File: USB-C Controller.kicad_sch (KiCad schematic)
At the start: 15 parts, among them J3 USB_C_Receptacle, Q5 AO4459, U3 STUSB4500QTR

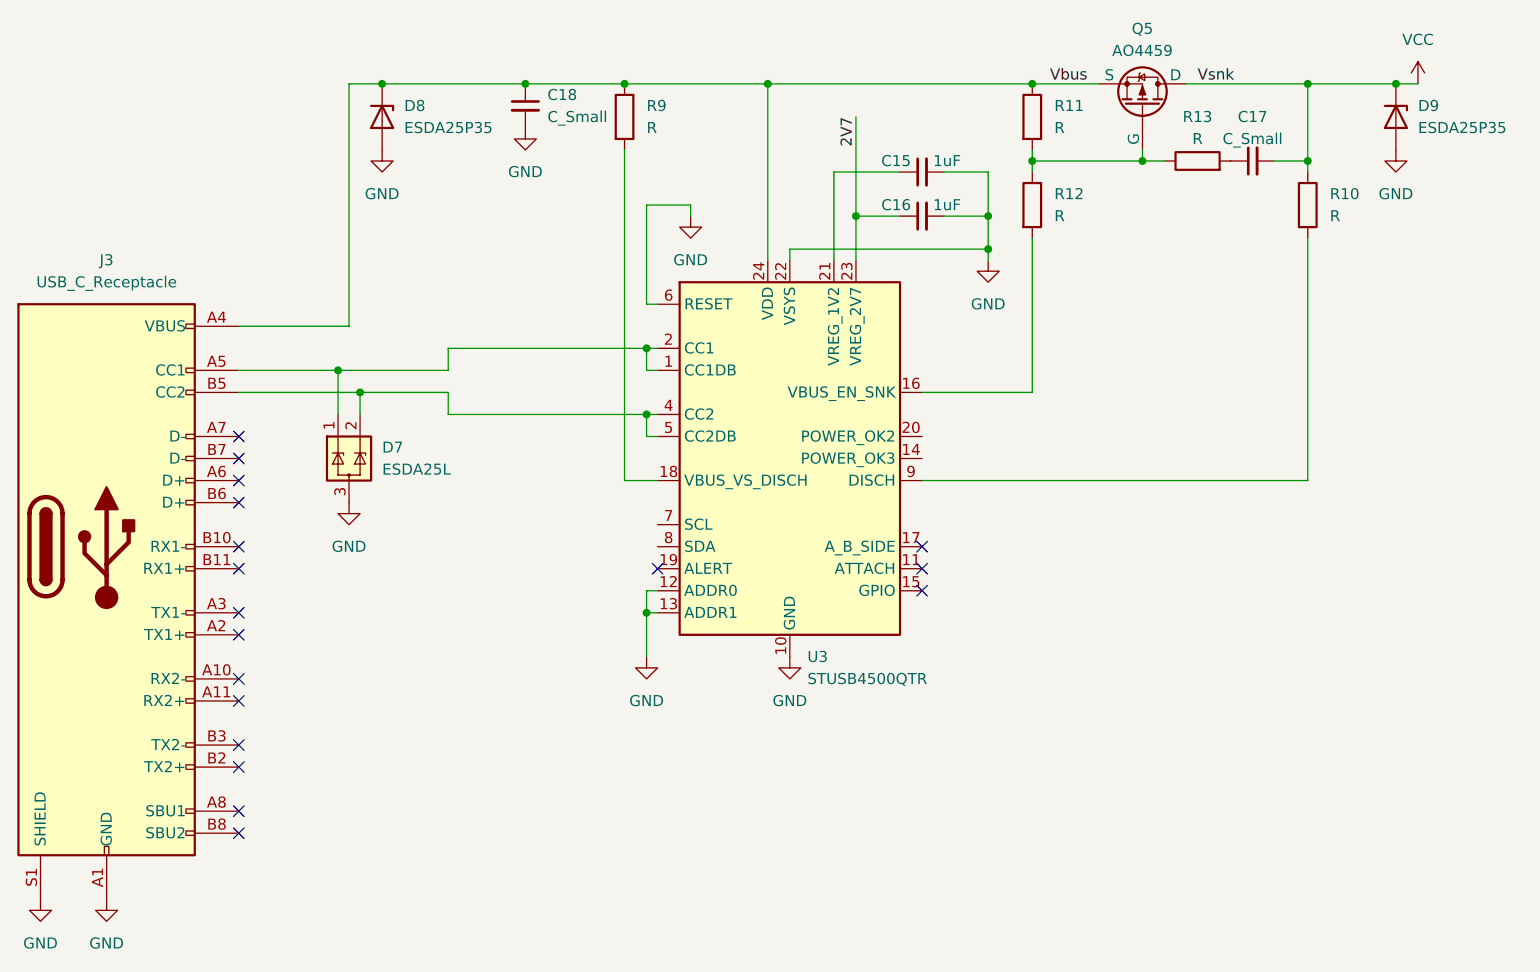
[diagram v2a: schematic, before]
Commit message: Add ESD protection, I2C header, and specify passives
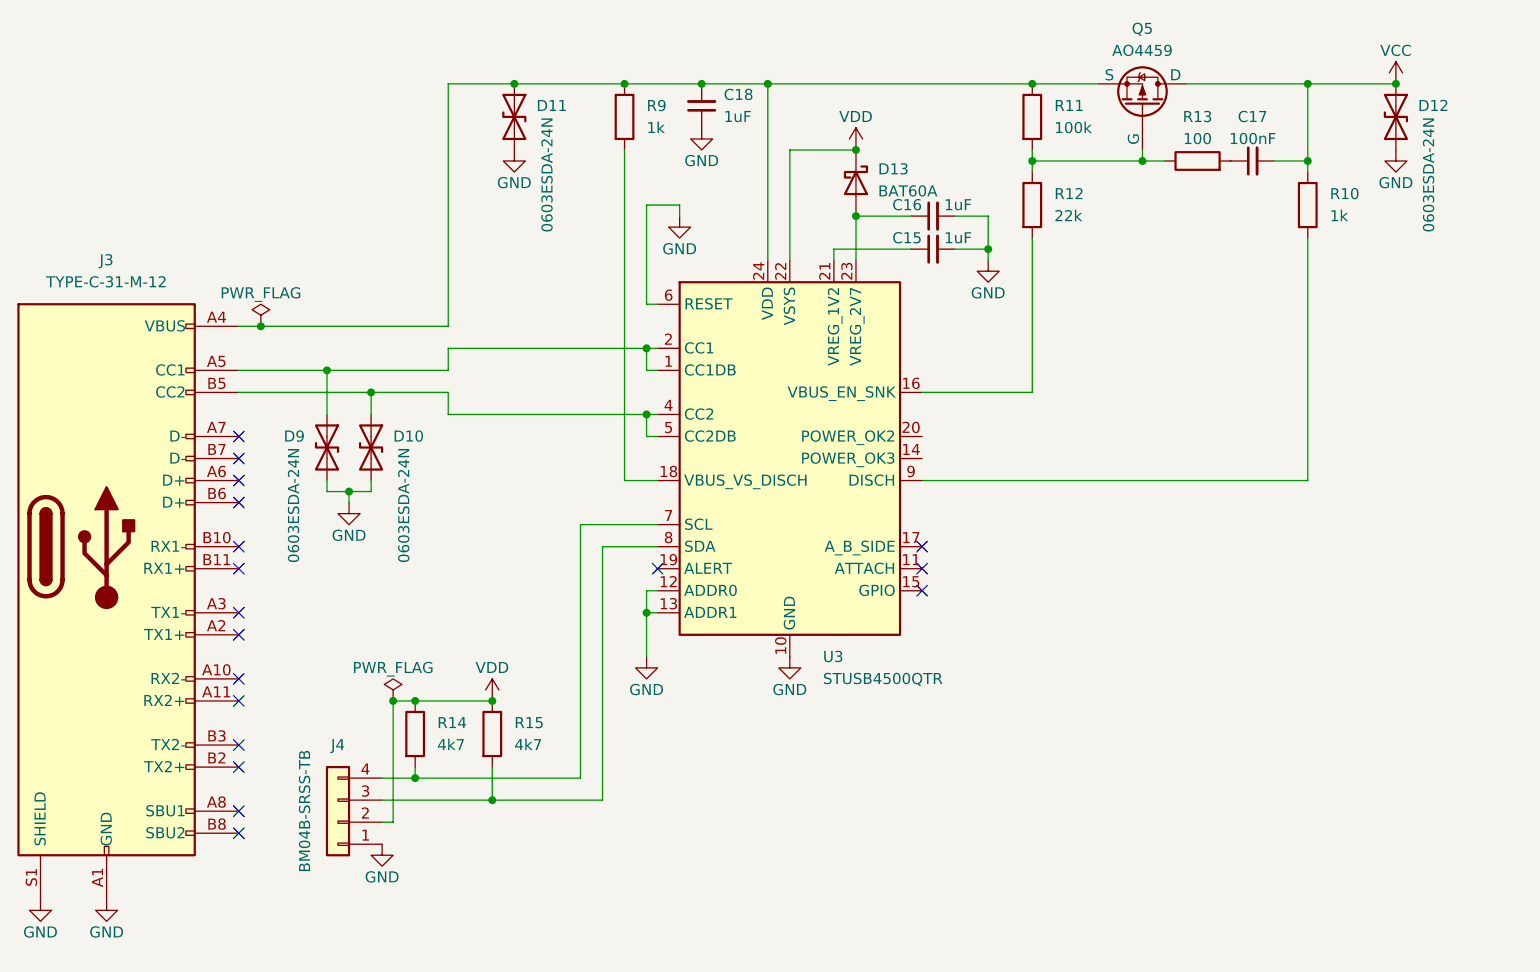
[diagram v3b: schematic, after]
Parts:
- removed D7: ESDA25L, Package_TO_SOT_SMD:SOT-23, symbol BRAUNIT Charger:ESDA25L
- removed D8, D9: ESDA25P35, symbol Device:D_Zener
- added D10, D11, D12, D9: 0603ESDA-24N, Diode_SMD:D_0603_1608Metric, symbol Device:D_TVS
- added D13: BAT60A, Diode_SMD:D_SOD-323, symbol Diode:BAT60A
- added J4: BM04B-SRSS-TB, Connector_JST:JST_SH_BM04B-SRSS-TB_1x04-1MP_P1.00mm_Vertical, symbol Connector_Generic:Conn_01x04
- added R14, R15: 4k7, Resistor_SMD:R_0603_1608Metric, symbol Device:R
- C17: value C_Small -> 100nF; footprint (none) -> Capacitor_SMD:C_0603_1608Metric; LCSC (none) -> C14663
- C18: value C_Small -> 1uF; footprint (none) -> Capacitor_SMD:C_0805_2012Metric; LCSC (none) -> C91185
- J3: value USB_C_Receptacle -> TYPE-C-31-M-12
- R10, R9: value R -> 1k; footprint (none) -> Resistor_SMD:R_0603_1608Metric; LCSC (none) -> C22548
- R11: value R -> 100k; footprint (none) -> Resistor_SMD:R_0603_1608Metric; LCSC (none) -> C14675
- R12: value R -> 22k; footprint (none) -> Resistor_SMD:R_0603_1608Metric; LCSC (none) -> C114065
- R13: value R -> 100; footprint (none) -> Resistor_SMD:R_0603_1608Metric; LCSC (none) -> C105588
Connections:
- net GND: now also C18.1, D10.2 (A2), D11.2 (A2), D12.2 (A2), D9.2 (A2), J4.1 (Pin_1); no longer C18.2, U3.22 (VSYS)
- net VCC: now also D12.1 (A1)
- net at J3.A5 (CC1), U3.1 (CC1DB), U3.2 (CC1): now also D9.1 (A1)
- net at J3.B5 (CC2), U3.4 (CC2), U3.5 (CC2DB): now also D10.1 (A1)
- net at U3.7 (SCL): now also J4.4 (Pin_4), R14.2
- net at U3.8 (SDA): now also J4.3 (Pin_3), R15.2
- net 2V7: no longer names the net of C16.1, U3.23 (VREG_2V7)
- net 2V7: now also D13.2 (A)
- net Vbus: no longer names the net of J3.A4 (VBUS), J3.A9 (VBUS), J3.B4 (VBUS), J3.B9 (VBUS), Q5.1 (S), Q5.2 (S), Q5.3 (S), R11.1, R9.1, U3.24 (VDD)
- net Vbus: now also C18.2, D11.1 (A1); no longer C18.1
- new net VDD: D13.1 (K), J4.2 (Pin_2), R14.1, R15.1, U3.22 (VSYS)
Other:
- moved on the sheet: C15, C16, C18

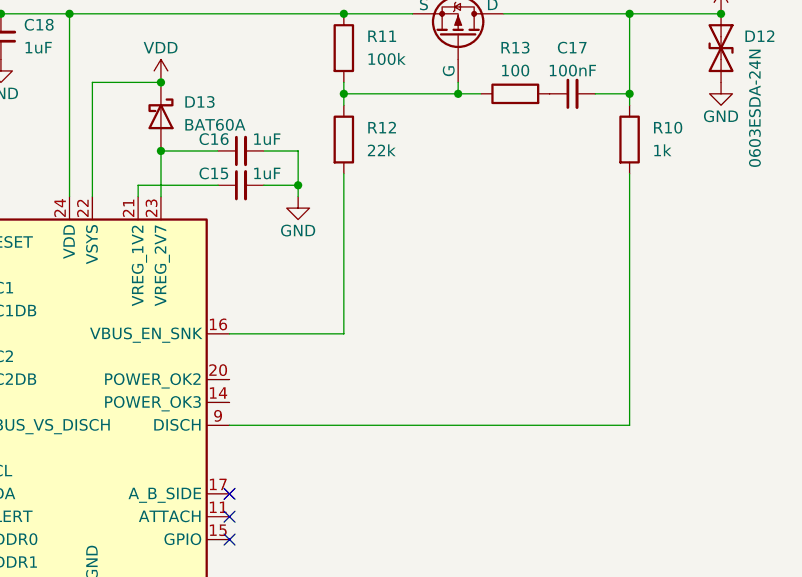
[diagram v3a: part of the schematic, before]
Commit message: Add USB-C status indicator LED and right charger enable
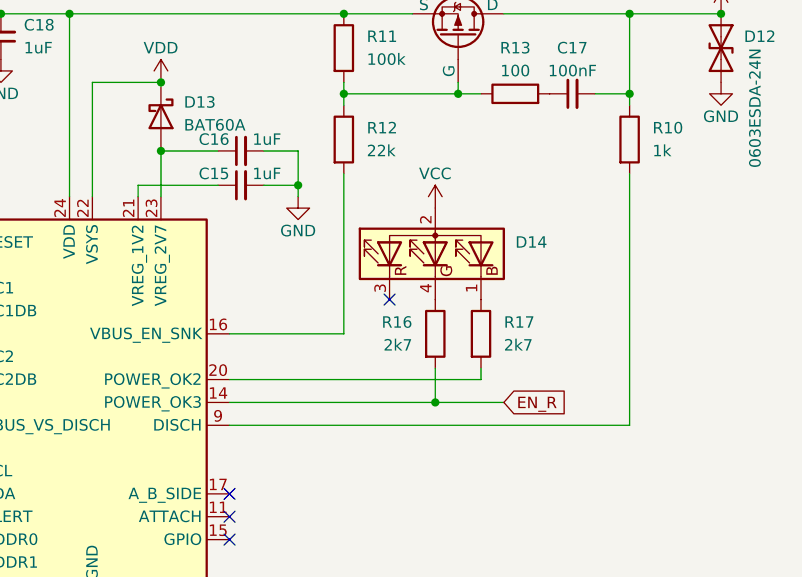
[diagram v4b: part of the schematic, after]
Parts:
- added D14: (no value), symbol Device:LED_BARG
- added R16, R17: 2k7, Resistor_SMD:R_0603_1608Metric, symbol Device:R
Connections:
- net VCC: now also D14.2 (A)
- net EN_R: now reaches U3.14 (POWER_OK3)
- net EN_R: now also R16.2
- net at U3.20 (POWER_OK2): now also R17.2
- new net: D14.1 (BK), R17.1
- new net: D14.4 (GK), R16.1
- no-connect marks 18 -> 19
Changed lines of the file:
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@@
   (junction (at 184.15 76.2) (diameter 0) (color 0 0 0 0)
   )
+  (junction (at 194.31 110.49) (diameter 0) (color 0 0 0 0)
+  )
   (junction (at 113.03 147.32) (diameter 0) (color 0 0 0 0)
   )
@@
   (junction (at 163.83 82.55) (diameter 0) (color 0 0 0 0)
   )
+  (no_connect (at 189.23 99.06))
   (no_connect (at 92.71 151.13))
   (no_connect (at 92.71 153.67))
@@
     (stroke (width 0) (type default) (color 0 0 0 0))
   )
+  (wire (pts (xy 171.45 110.49) (xy 194.31 110.49))
+    (stroke (width 0) (type default) (color 0 0 0 0))
+  )
   (wire (pts (xy 132.08 118.11) (xy 140.97 118.11))
     (stroke (width 0) (type default) (color 0 0 0 0))
@@
     (stroke (width 0) (type default) (color 0 0 0 0))
   )
+  (wire (pts (xy 194.31 110.49) (xy 201.93 110.49))
+    (stroke (width 0) (type default) (color 0 0 0 0))
+  )
   (wire (pts (xy 184.15 76.2) (xy 184.15 77.47))
     (stroke (width 0) (type default) (color 0 0 0 0))
@@
     (stroke (width 0) (type default) (color 0 0 0 0))
   )
+  (wire (pts (xy 171.45 107.95) (xy 199.39 107.95))
+    (stroke (width 0) (type default) (color 0 0 0 0))
+  )
   (wire (pts (xy 134.62 149.86) (xy 134.62 120.65))
     (stroke (width 0) (type default) (color 0 0 0 0))
@@
     (stroke (width 0) (type default) (color 0 0 0 0))
   )
+  (wire (pts (xy 194.31 106.68) (xy 194.31 110.49))
+    (stroke (width 0) (type default) (color 0 0 0 0))
+  )
   (wire (pts (xy 215.9 67.31) (xy 215.9 76.2))
     (stroke (width 0) (type default) (color 0 0 0 0))
@@
     (stroke (width 0) (type default) (color 0 0 0 0))
   )
+  (wire (pts (xy 199.39 107.95) (xy 199.39 106.68))
+    (stroke (width 0) (type default) (color 0 0 0 0))
+  )
   (wire (pts (xy 175.26 82.55) (xy 179.07 82.55))
     (stroke (width 0) (type default) (color 0 0 0 0))
@@
   (wire (pts (xy 140.97 107.95) (xy 139.7 107.95))
     (stroke (width 0) (type default) (color 0 0 0 0))
+  )
+  (global_label "EN_R" (shape input) (at 201.93 110.49 0) (fields_autoplaced)
+    (effects (font (size 1.27 1.27)) (justify left))
+    (property "Intersheet References" "${INTERSHEET_REFS}" (id 0) (at 209.0602 110.4106 0)
+      (effects (font (size 1.27 1.27)) (justify left) hide)
+    )
+  )
+  (symbol (lib_id "Device:R") (at 199.39 102.87 0) (unit 1)
+    (in_bom yes) (on_board yes) (fields_autoplaced)
+    (property "Reference" "R17" (id 0) (at 201.93 101.5999 0)
+      (effects (font (size 1.27 1.27)) (justify left))
+    )
+    (property "Value" "2k7" (id 1) (at 201.93 104.1399 0)
+      (effects (font (size 1.27 1.27)) (justify left))
+    )
+    (property "Footprint" "Resistor_SMD:R_0603_1608Metric" (id 2) (at 197.612 102.87 90)
+      (effects (font (size 1.27 1.27)) hide)
+    )
+    (property "Datasheet" "~" (id 3) (at 199.39 102.87 0)
+      (effects (font (size 1.27 1.27)) hide)
+    )
+    (property "LCSC" "C114612" (id 4) (at 199.39 102.87 0)
+      (effects (font (size 1.27 1.27)) hide)
+    )
+    (pin "1")
+    (pin "2")
   )
   (symbol (lib_id "power:GND") (at 226.06 74.93 0) (unit 1)
@@
     (pin "1")
   )
+  (symbol (lib_id "Device:LED_BARG") (at 194.31 93.98 90) (unit 1)
+    (in_bom yes) (on_board yes)
+    (property "Reference" "D14" (id 0) (at 203.2 92.71 90)
+      (effects (font (size 1.27 1.27)) (justify right))
+    )
+    (property "Value" "" (id 1) (at 196.85 88.9 90)
+      (effects (font (size 1.27 1.27)) (justify right))
+    )
+    (property "Footprint" "" (id 2) (at 195.58 93.98 0)
+      (effects (font (size 1.27 1.27)) hide)
+    )
+    (property "Datasheet" "~" (id 3) (at 195.58 93.98 0)
+      (effects (font (size 1.27 1.27)) hide)
+    )
+    (property "LCSC" "C389528" (id 4) (at 194.31 93.98 90)
+      (effects (font (size 1.27 1.27)) hide)
+    )
+    (pin "1")
+    (pin "2")
+    (pin "3")
+    (pin "4")
+  )
   (symbol (lib_id "Device:R") (at 203.2 76.2 90) (unit 1)
     (in_bom yes) (on_board yes)
@@
     (pin "2")
   )
+  (symbol (lib_id "power:VCC") (at 194.31 88.9 0) (unit 1)
+    (in_bom yes) (on_board yes)
+    (property "Reference" "#PWR0137" (id 0) (at 194.31 92.71 0)
+      (effects (font (size 1.27 1.27)) hide)
+    )
+    (property "Value" "VCC" (id 1) (at 194.31 85.09 0))
+    (property "Footprint" "" (id 2) (at 194.31 88.9 0)
+      (effects (font (size 1.27 1.27)) hide)
+    )
+    (property "Datasheet" "" (id 3) (at 194.31 88.9 0)
+      (effects (font (size 1.27 1.27)) hide)
+    )
+    (pin "1")
+  )
   (symbol (lib_id "Device:D_TVS") (at 102.87 109.22 270) (unit 1)
     (in_bom yes) (on_board yes)
@@
     )
     (pin "1")
+    (pin "2")
+  )
+  (symbol (lib_id "Device:R") (at 194.31 102.87 0) (unit 1)
+    (in_bom yes) (on_board yes)
+    (property "Reference" "R16" (id 0) (at 191.77 101.6 0)
+      (effects (font (size 1.27 1.27)) (justify right))
+    )
+    (property "Value" "2k7" (id 1) (at 191.77 104.14 0)
+      (effects (font (size 1.27 1.27)) (justify right))
+    )
+    (property "Footprint" "Resistor_SMD:R_0603_1608Metric" (id 2) (at 192.532 102.87 90)
+      (effects (font (size 1.27 1.27)) hide)
+    )
+    (property "Datasheet" "~" (id 3) (at 194.31 102.87 0)
+      (effects (font (size 1.27 1.27)) hide)
+    )
+    (property "LCSC" "C114612" (id 4) (at 194.31 102.87 0)
+      (effects (font (size 1.27 1.27)) hide)
+    )
+    (pin "1")

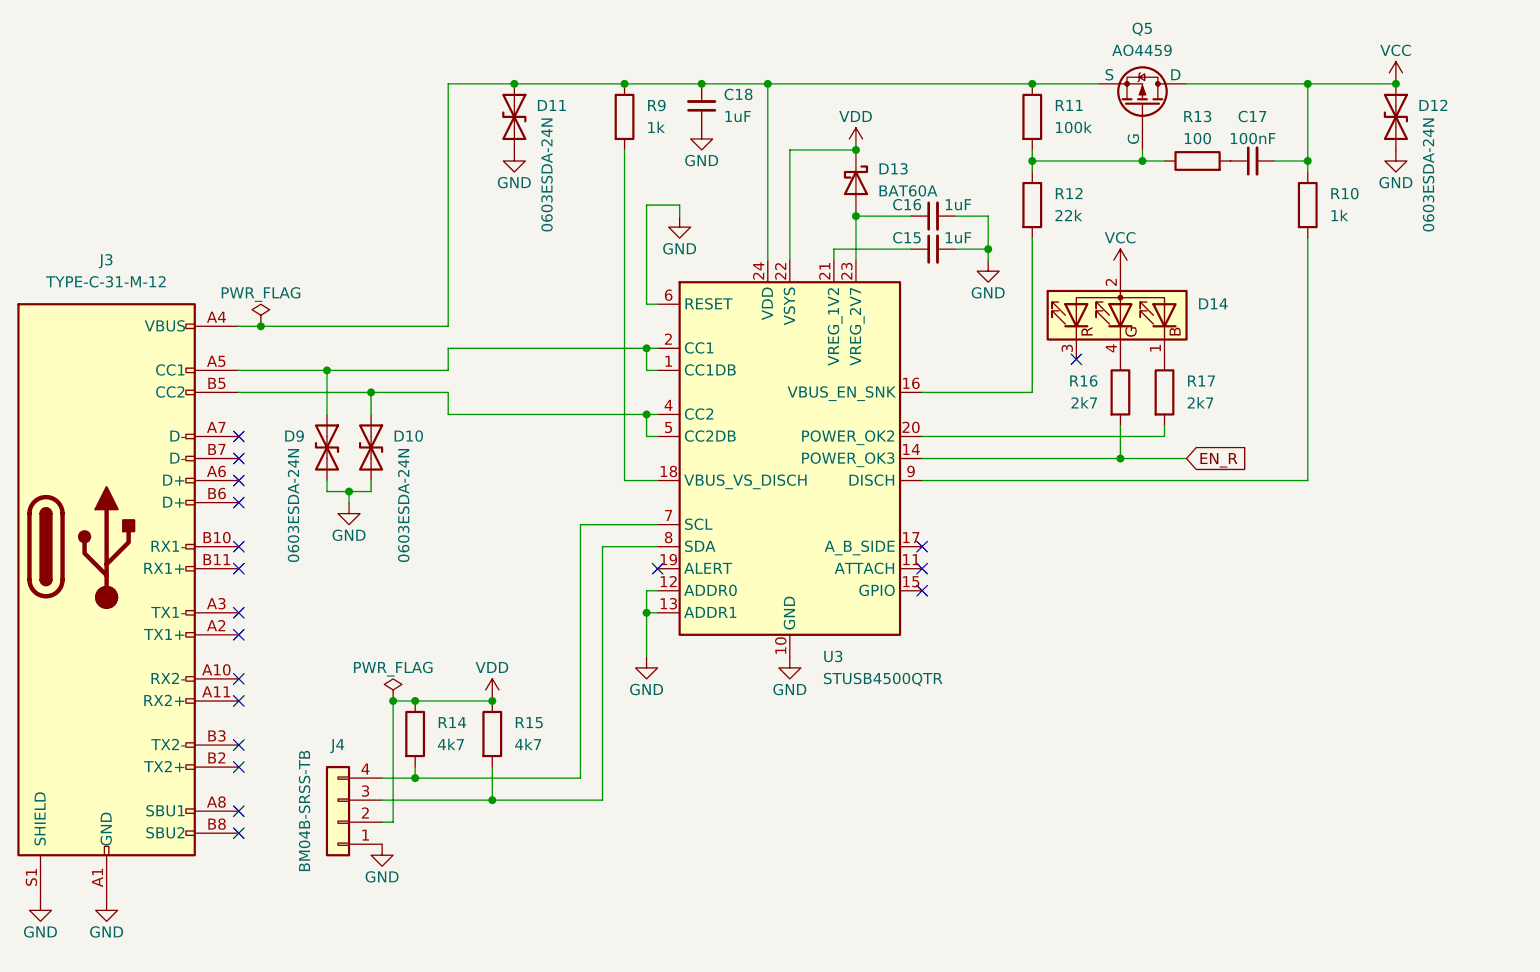
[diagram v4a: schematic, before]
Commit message: Replace USB-C connector with USB 2.0 version
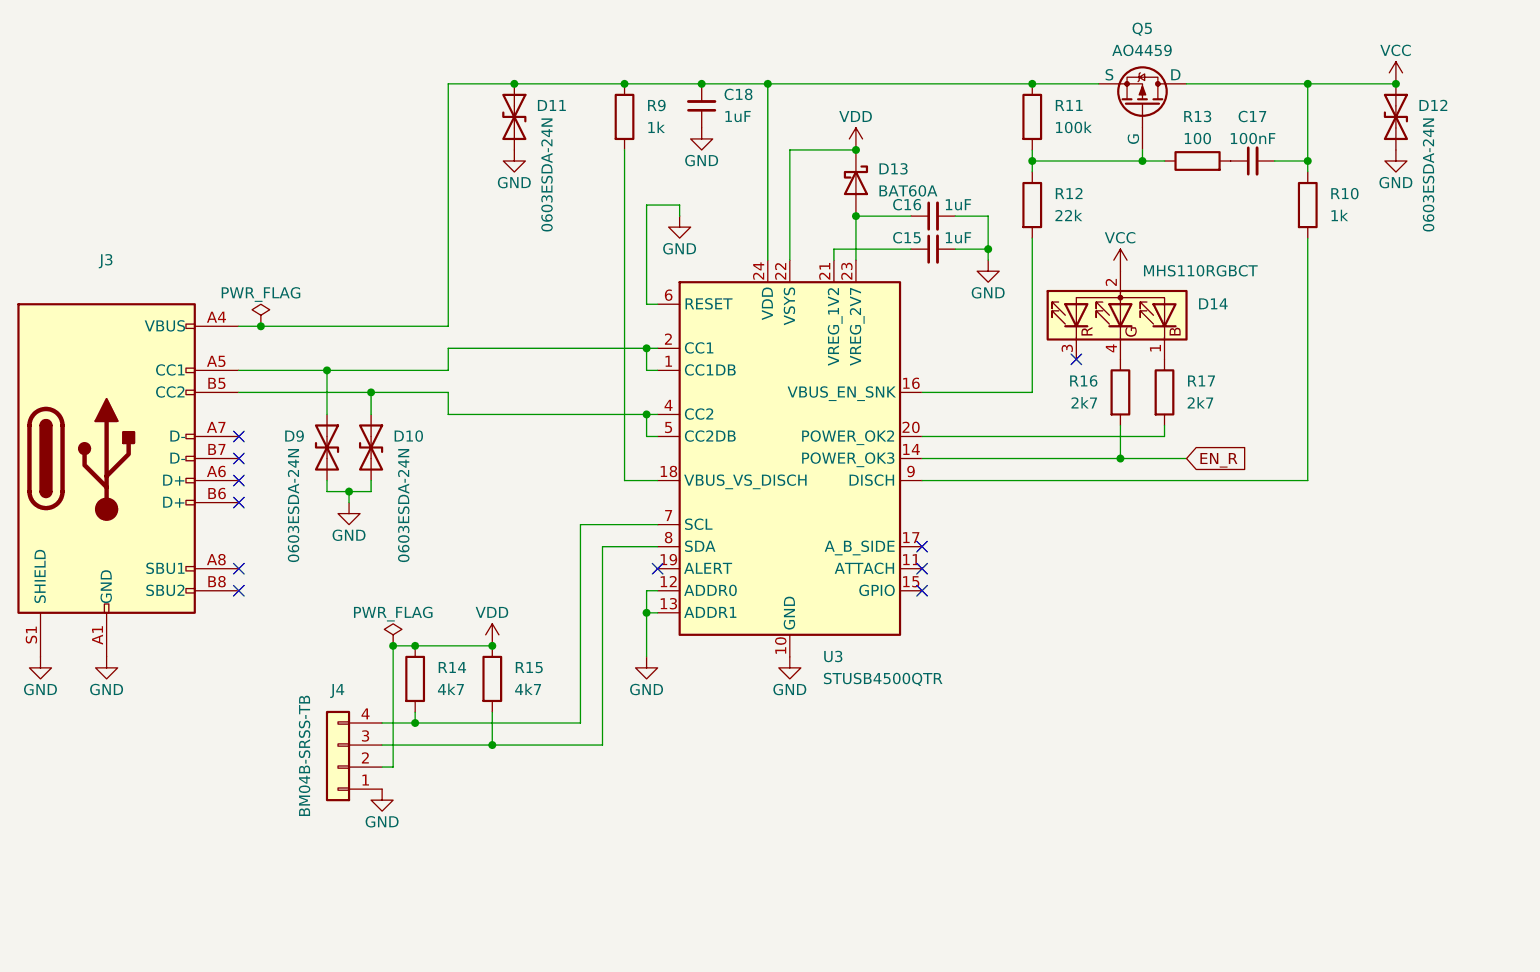
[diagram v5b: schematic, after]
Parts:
- D14: value (none) -> MHS110RGBCT; footprint (none) -> BRAUNIT Charger:LED_RGB_Meihua_MHS110RGBCT
- J3: value TYPE-C-31-M-12 -> (none); footprint Connector_USB:USB_C_Receptacle_HRO_TYPE-C-31-M-12 -> (none); symbol Connector:USB_C_Receptacle -> Connector:USB_C_Receptacle_USB2.0
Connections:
- no-connect marks 19 -> 11
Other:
- moved on the sheet: J4, R14, R15
